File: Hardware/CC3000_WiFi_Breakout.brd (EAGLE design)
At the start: 35.6 x 40.6 mm, 33 parts, among them J1 U.FL, U1 LM1117, U3 74HC4050, U5 CC3000

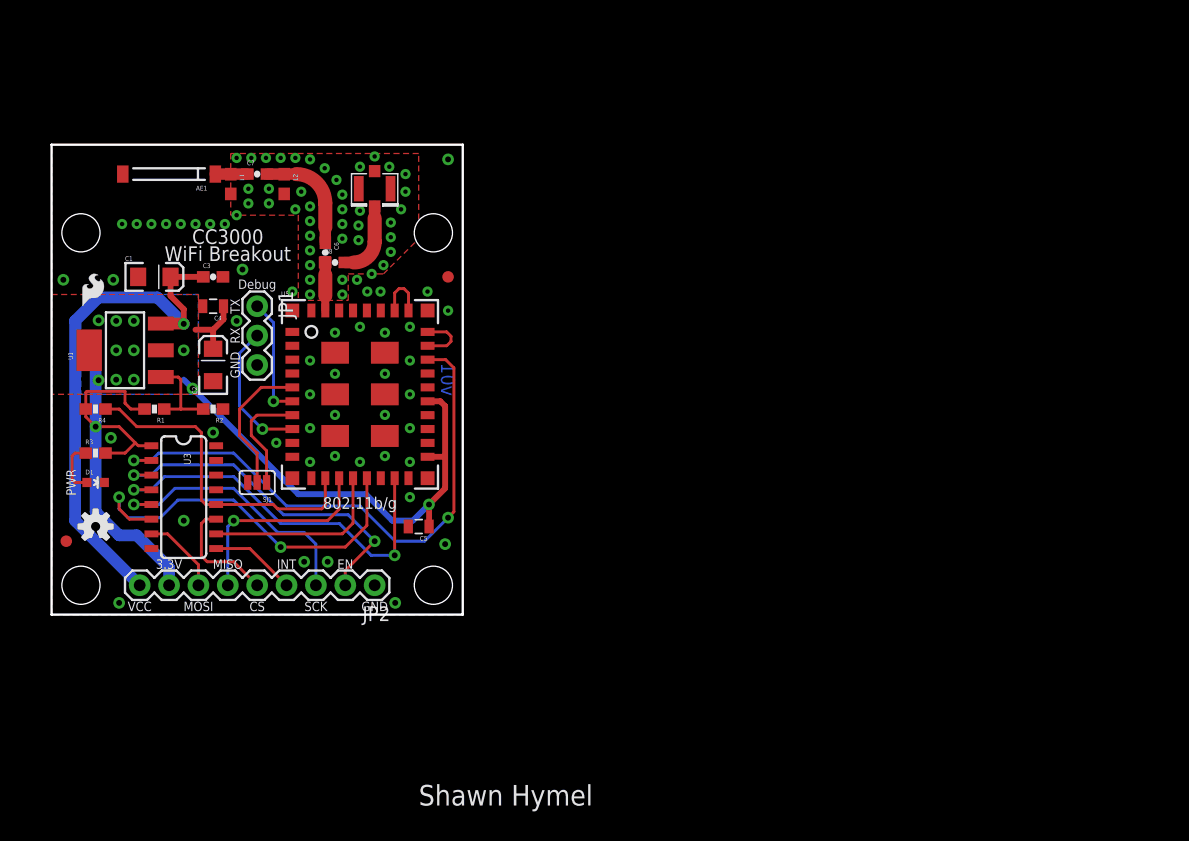
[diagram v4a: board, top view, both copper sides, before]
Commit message: Changed layout for board
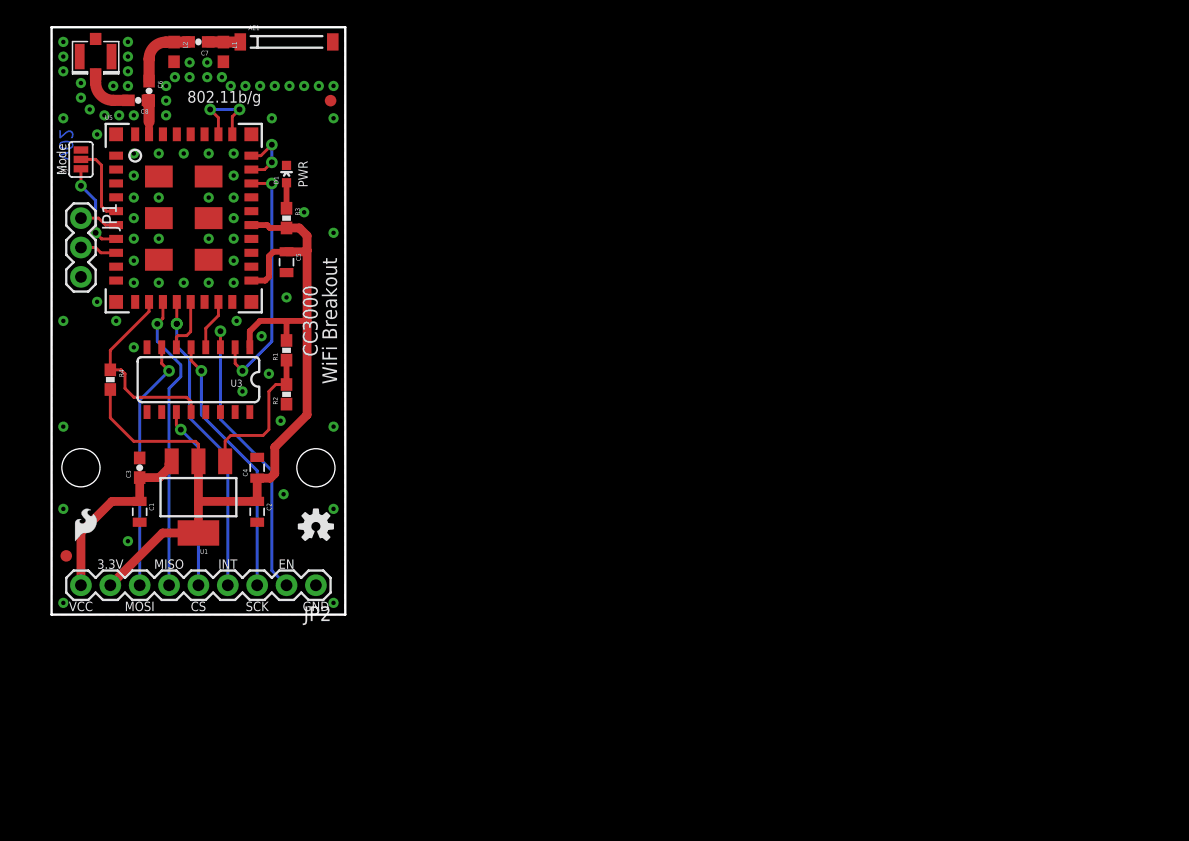
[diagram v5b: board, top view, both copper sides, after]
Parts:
- removed STANDOFF3, STANDOFF4: STAND-OFF, SparkFun-Electromechanical:STAND-OFF
- C1, C2: device SparkFun-Capacitors:EIA3216 -> SparkFun-Capacitors:0805
- moved SJ1 31.8 mm to (2.54, 39.4), turned to 90 degrees
- moved D1 31.4 mm to (20.3, 38.1), turned to 0 degrees
- moved J1 26.7 mm to (3.81, 48.3)
- moved R3 26.2 mm to (20.3, 34.3), turned to 270 degrees
- moved C5 25.6 mm to (20.3, 30.5), turned to 270 degrees
- moved STANDOFF1 22.7 mm to (22.9, 12.7)
- moved C8 22.0 mm to (7.49, 44.5), turned to 180 degrees
- moved U5 21.6 mm to (11.4, 34.3)
- moved C6 20.7 mm to (8.43, 45.3)
- moved C1 20.4 mm to (7.62, 8.89), turned to 270 degrees
- moved LOGO3 20.3 mm to (2.03, 6.35)
- moved STANDOFF2 20.3 mm to (2.54, 12.7)
- moved LOGO1 19.1 mm to (22.9, 7.62)
- moved FRAME1 18.9 mm to (-17.8, -10.2)
- moved FID1 18.3 mm to (24.1, 44.5)
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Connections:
- net CS renamed CS_5V
- net EN renamed EN_5V
- net MOSI renamed MOSI_5V
- net SCK renamed SCK_5V
- net SPI_MISO renamed MISO_3.3V
- net SPI_MOSI renamed MOSI_3.3V
- net SPI_SCK renamed SCK_3.3V
- net WIFI_CS renamed CS_3.3V
- net WIFI_EN renamed EN_3.3V
- removed net INT: JP2.4, U3.9
- removed net WIFI_INT: U3.10, U5.P$14
- new net INT_3.3V: JP2.4, U5.P$14
- net 3.3V: now also C2.1; no longer C2.A
- net GND: now also C1.2, C2.2; no longer C1.C, C2.C
- net VCC: now also C1.1; no longer C1.A
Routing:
- net SCK_3.3V: track 34.0 -> 4.37 mm, vias 2 -> 0
- net VCC: track 45.7 -> 16.4 mm, vias 1 -> 0
- net MOSI_3.3V: track 34.1 -> 4.88 mm, vias 2 -> 0
- net EN_3.3V: track 48.7 -> 21.3 mm
- net INT_3.3V: track 0.00 -> 26.3 mm, vias 0 -> 2
- net WIFI_INT: track 16.1 -> 0.00 mm
- net MOSI_5V: track 6.95 -> 21.9 mm, vias 0 -> 1
- net CS_3.3V: track 28.5 -> 17.0 mm
- net WIFI_RX: track 12.1 -> 3.23 mm, vias 1 -> 0
- net 3.3V: track 87.8 -> 79.3 mm, vias 12 -> 0
- net MISO_3.3V: track 18.0 -> 26.0 mm
- net INT: track 7.41 -> 0.00 mm
- net WIFI_TX: track 10.4 -> 3.29 mm, vias 1 -> 0
- net CS_5V: track 10.1 -> 15.8 mm, vias 0 -> 1
- net N$2: track 7.74 -> 13.1 mm
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- removed copper zone on layer 1, net 3.3V
- removed copper zone on layer 16, net 3.3V
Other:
- board size 35.6 x 40.6 mm -> 25.4 x 50.8 mm
- board text added: "Mode"
- board text added: "v02"
- board text removed: "v01"

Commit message: Redid layout. Again.
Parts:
- removed LOGO2: LOGO-SFENEW, SparkFun-Aesthetics:SFE-NEW-WEBLOGO
- added LOGO4: SFE_LOGO_NAME_FLAME.1_INCH, SparkFun-Aesthetics:SFE_LOGO_NAME_FLAME_.1
- moved LOGO1 30.5 mm to (21.6, 38.1)
- moved LOGO3 15.2 mm to (17.3, 6.35)
- moved R4 12.0 mm to (8.89, 8.89)
- moved C2 10.2 mm to (22.9, 17.8), turned to 90 degrees
- moved U1 7.18 mm to (17.8, 15.2)
- moved U3 7.18 mm to (7.62, 15.2)
- moved AE1 6.35 mm to (20.3, 43.2)
- moved C7 6.35 mm to (12.7, 43.2)
- moved L1 6.35 mm to (14.9, 42.3)
- moved L2 6.35 mm to (10.6, 42.3)
- moved C1 6.35 mm to (14.0, 8.89)
- moved FID2 6.35 mm to (1.27, 11.4)
- moved C3 5.39 mm to (11.4, 8.89), turned to 270 degrees
- moved C4 5.24 mm to (22.9, 14.0), turned to 270 degrees
- moved D1 5.24 mm to (21.6, 33.0), turned to 90 degrees
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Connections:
- net 3.3V: now also JP2.7; no longer JP2.8
- net CS_5V: now also JP2.4; no longer JP2.5
- net EN_5V: now also JP2.1; no longer JP2.2
- net GND: now also JP2.9; no longer JP2.1
- net INT_3.3V: now also JP2.3; no longer JP2.4
- net MISO_3.3V: now also JP2.5; no longer JP2.6
- net MOSI_5V: now also JP2.6; no longer JP2.7
- net SCK_5V: now also JP2.2; no longer JP2.3
- net VCC: now also JP2.8; no longer JP2.9
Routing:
- net 3.3V: track 79.3 -> 60.2 mm, vias 0 -> 11
- net VCC: track 16.4 -> 28.4 mm
- net SCK_3.3V: track 4.37 -> 9.30 mm
- net MOSI_3.3V: track 4.88 -> 9.51 mm
- net N$2: track 13.1 -> 8.78 mm
- net EN_5V: track 25.7 -> 21.9 mm
- net MISO_3.3V: track 26.0 -> 23.5 mm
- net INT_3.3V: track 26.3 -> 24.0 mm, vias 2 -> 1
- net CS_5V: track 15.8 -> 18.1 mm
- net SCK_5V: track 22.9 -> 21.0 mm
- net EN_3.3V: track 21.3 -> 22.9 mm
- net N$5: track 5.95 -> 4.63 mm
- net MOSI_5V: track 21.9 -> 20.9 mm
- net CS_3.3V: track 17.0 -> 17.5 mm, vias 0 -> 2
- added copper zone on layer 1, net 3.3V
- added copper zone on layer 16, net 3.3V
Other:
- board size 25.4 x 50.8 mm -> 25.4 x 45.7 mm
- board text added: "CC3000 WiFi Breakout"
- board text removed: "CC3000"
- board text removed: "WiFi Breakout"

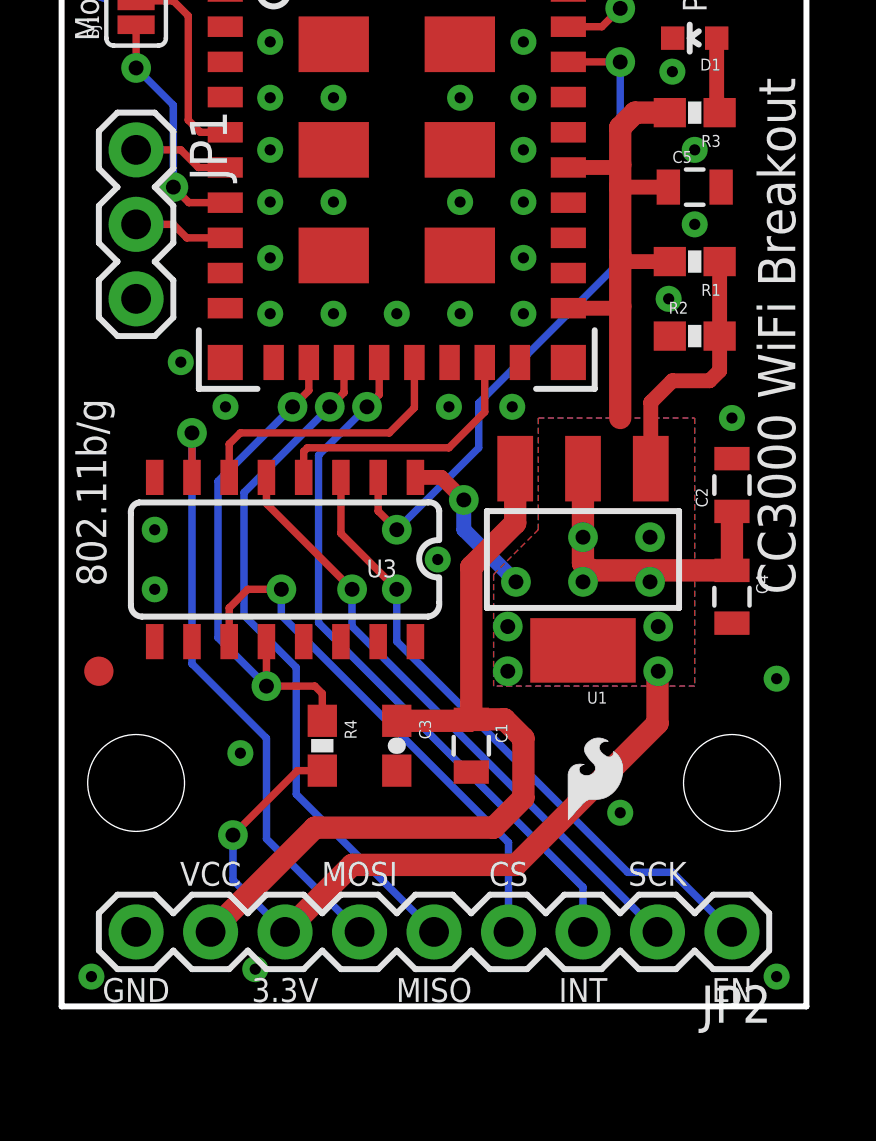
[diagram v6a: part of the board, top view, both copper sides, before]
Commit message: Moved headers closer to board edge
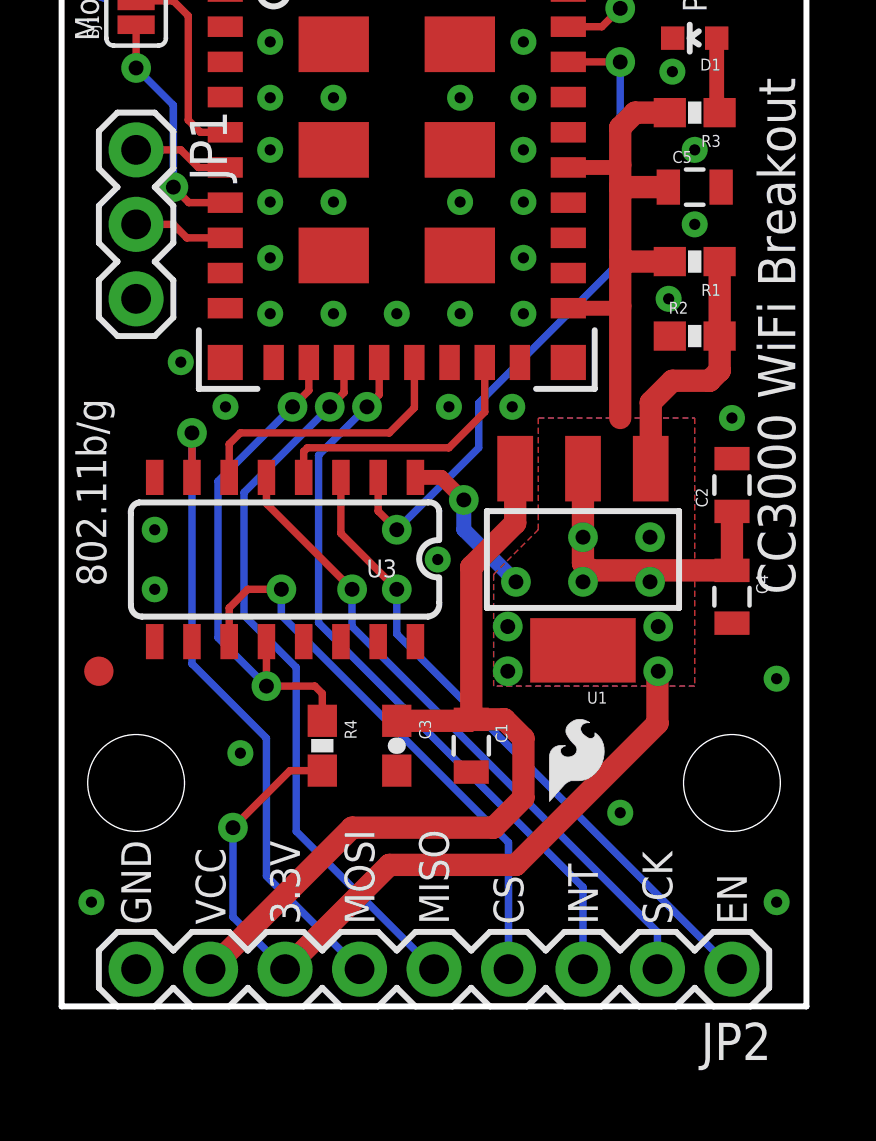
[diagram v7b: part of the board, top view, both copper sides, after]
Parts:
- moved JP2 1.27 mm to (22.9, 1.27)
- moved LOGO3 0.90 mm to (16.6, 6.99)
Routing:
- net 3.3V: track 60.2 -> 62.1 mm
- net SCK_5V: track 21.0 -> 22.3 mm
- net MISO_3.3V: track 23.5 -> 24.8 mm
- net INT_3.3V: track 24.0 -> 25.3 mm
- net MOSI_5V: track 20.9 -> 22.2 mm
- net CS_5V: track 18.1 -> 19.4 mm
- net VCC: track 28.4 -> 28.9 mm

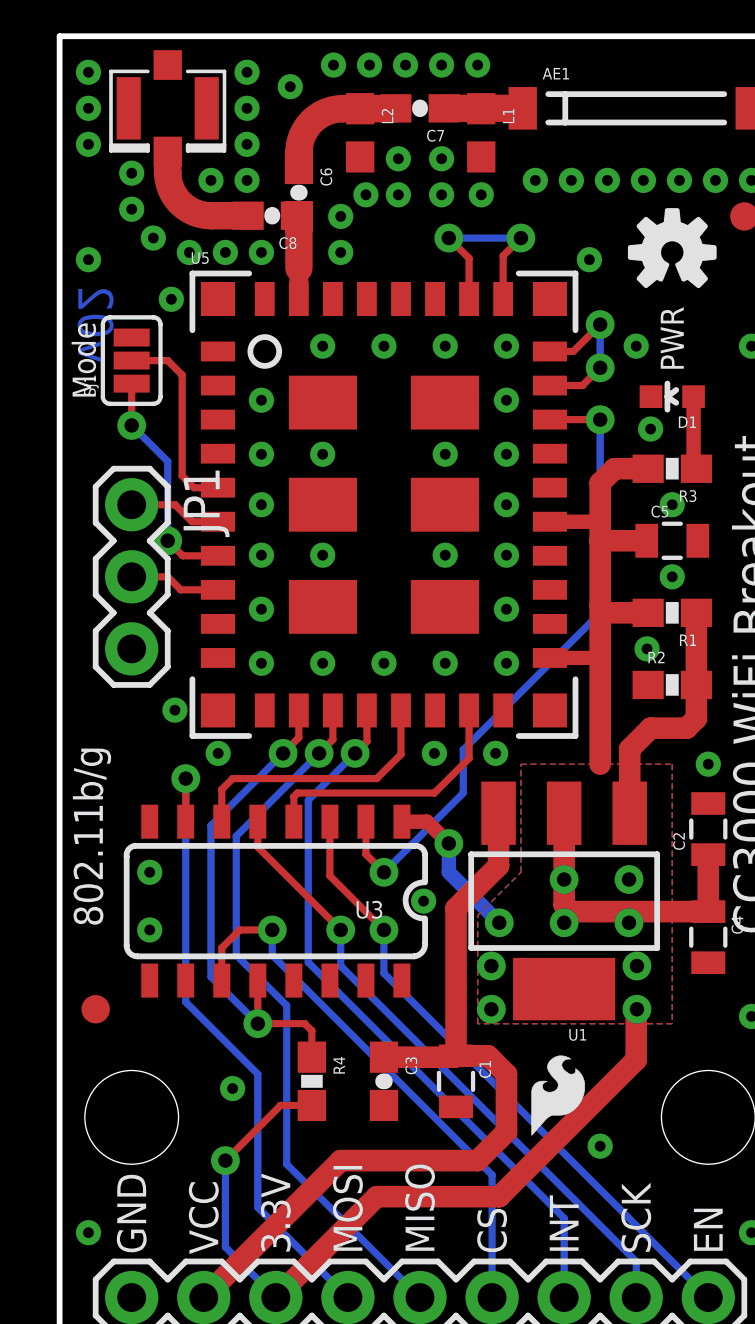
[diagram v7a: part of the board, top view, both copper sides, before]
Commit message: Moved SS Flame down, added pin marker for U.FL in SS
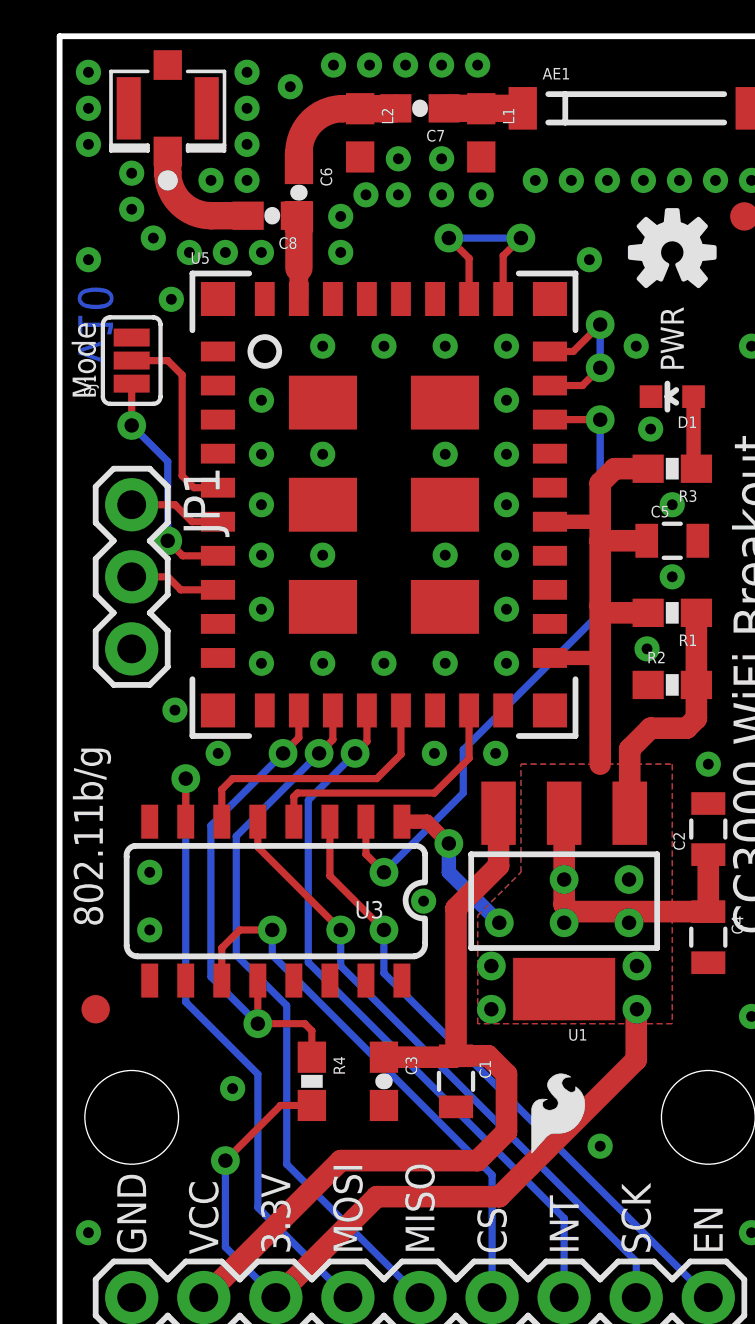
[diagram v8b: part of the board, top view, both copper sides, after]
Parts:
- moved LOGO3 0.64 mm to (16.6, 6.35)
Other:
- board text added: "v10"
- board text removed: "v02"
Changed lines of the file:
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@@
 <setting verticaltext="up"/>
 </settings>
-<grid distance="0.05" unitdist="inch" unit="inch" style="dots" multiple="1" display="yes" altdistance="0.025" altunitdist="inch" altunit="inch"/>
+<grid distance="0.01" unitdist="inch" unit="inch" style="dots" multiple="1" display="yes" altdistance="0.005" altunitdist="inch" altunit="inch"/>
 <layers>
 <layer number="1" name="Top" color="4" fill="1" visible="yes" active="yes"/>
@@
 <text x="5.715" y="26.67" size="0.8128" layer="22" font="vector" ratio="15" rot="MR270" align="center">Debug</text>
 <text x="12.7" y="-10.16" size="1.778" layer="51" font="vector">Shawn Hymel</text>
-<text x="1.27" y="35.56" size="1.2192" layer="16" font="vector" ratio="15" rot="MR270" align="center">v02</text>
+<text x="1.27" y="35.56" size="1.2192" layer="16" font="vector" ratio="15" rot="MR270" align="center">v10</text>
 <text x="24.384" y="22.86" size="1.27" layer="21" font="vector" ratio="15" rot="R90" align="center">CC3000 WiFi Breakout</text>
 <text x="1.016" y="17.526" size="1.016" layer="21" font="vector" ratio="15" rot="R90" align="center">802.11b/g</text>
@@
 <text x="1.27" y="34.29" size="0.8128" layer="21" font="vector" ratio="15" rot="R270" align="top-center">Mode</text>
 <text x="24.384" y="22.86" size="1.27" layer="22" font="vector" ratio="15" rot="MR90" align="center">CC3000 WiFi Breakout</text>
+<circle x="3.81" y="40.64" radius="0.179603125" width="0.3556" layer="21"/>
 </plain>
 <attributes>
@@
 <element name="FID2" library="SparkFun-Aesthetics" package="FIDUCIAL-1X2" value="FIDUCIAL1X2" x="1.27" y="11.43"/>
 <element name="LOGO1" library="SparkFun-Aesthetics" package="OSHW-LOGO-S" value="OSHW-LOGOS" x="21.59" y="38.1"/>
-<element name="LOGO3" library="SparkFun-Aesthetics" package="SFE-LOGO-FLAME" value="LOGO-SFESK" x="16.637" y="6.985"/>
+<element name="LOGO3" library="SparkFun-Aesthetics" package="SFE-LOGO-FLAME" value="LOGO-SFESK" x="16.637" y="6.35"/>
 <element name="JP2" library="SparkFun-Connectors" package="1X09" value="M09" x="22.86" y="1.27" rot="R180"/>
 <element name="STANDOFF1" library="SparkFun-Electromechanical" package="STAND-OFF" value="STAND-OFF" x="22.86" y="7.62" rot="R90"/>
